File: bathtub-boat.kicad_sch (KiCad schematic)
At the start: 3 parts, among them U1 esp-01m, U2 tp4056

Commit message: Add components
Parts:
- added BT2: Battery_Cell, Connector_JST:JST_PH_S2B-PH-SM4-TB_1x02-1MP_P2.00mm_Horizontal, symbol Device:Battery_Cell
- added BT3: Battery_Cell, Connector_JST:JST_PH_B2B-PH-K_1x02_P2.00mm_Vertical, symbol Device:Battery_Cell
- added J1: I2C, Connector_JST:JST_SH_SM04B-SRSS-TB_1x04-1MP_P1.00mm_Horizontal, symbol Connector_Generic:Conn_01x04
- added J2: SPI, Connector_PinHeader_2.54mm:PinHeader_1x06_P2.54mm_Vertical, symbol Connector_Generic:Conn_01x06
- added SW1: MODE, Button_Switch_SMD:SW_Push_1P1T_NO_Vertical_Wuerth_434133025816, symbol Switch:SW_Push
- added SW2: RESET, Button_Switch_SMD:SW_Push_1P1T_NO_Vertical_Wuerth_434133025816, symbol Switch:SW_Push
- added SW4: A, Button_Switch_SMD:SW_Push_1P1T_NO_Vertical_Wuerth_434133025816, symbol Switch:SW_Push
- added U3: UA78M33_TO252, Package_TO_SOT_SMD:TO-252-2, symbol Regulator_Linear:KA78M05_TO252
- added U4: DS18B20, Package_TO_SOT_THT:TO-92_Inline_Wide, symbol Sensor_Temperature:DS18B20
- added U5: TTL, Connector_PinHeader_2.54mm:PinHeader_1x04_P2.54mm_Vertical, symbol ftdi-connector:TTL
- BT1: footprint (none) -> Connector_JST:JST_GH_BM02B-GHS-TBT_1x02-1MP_P1.25mm_Vertical
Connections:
- net +3V3: now also J1.2 (Pin_2), J2.2 (Pin_2), U3.3 (VO), U4.3 (VDD), U5.4 (VDD)
- net GND: now also U2.2 (IN-), U2.4 (O-), J1.1 (Pin_1), J2.1 (Pin_1), SW1.1, SW2.1, SW4.1, U3.2 (GND), U4.1 (GND), U5.1 (GND)
- net RX: now also U5.3 (TX)
- net TX: now also U5.2 (RX)
- net VBUS: now reaches U2.1 (IN+)
- net +5V: now reaches U2.3 (O+)
- net +5V: now also U3.1 (VI)
- net at BT1.1 (+), U2.5 (B+): now also BT2.1 (+), BT3.1 (+)
- net at BT1.2 (-), U2.6 (B-): now also BT2.2 (-), BT3.2 (-)
- net I2C_SDA: now reaches U1.10 (GP4)
- net I2C_SDA: now also J1.3 (Pin_3)
- net TEMP: now reaches U1.11 (GP9)
- net TEMP: now also U4.2 (DQ)
- net Neopixel: now reaches U1.12 (GP10)
- net I2C_SCL: now reaches U1.13 (GP5)
- net I2C_SCL: now also J1.4 (Pin_4)
- net SPI_MISO: now reaches U1.14 (GP12)
- net SPI_MISO: now also J2.3 (Pin_3)
- net SPI_CLK: now reaches U1.15 (GP14)
- net SPI_CLK: now also J2.5 (Pin_5)
- net at U1.17 (GP16): now also U1.18 (RST), SW2.2
- net SPI_MOSI: now reaches U1.5 (GP13)
- net SPI_MOSI: now also J2.4 (Pin_4)
- net SPI_CS: now reaches U1.6 (GP15)
- net SPI_CS: now also J2.6 (Pin_6)
- net BUTTON-A: now reaches U1.7 (GP2)
- net BUTTON-A: now also SW4.2
- net at U1.8 (GP0): now also SW1.2
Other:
- moved on the sheet: U2

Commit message: Prepare the pcb for next iteration
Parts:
- removed BT2: Battery_Cell, Connector_JST:JST_PH_S2B-PH-SM4-TB_1x02-1MP_P2.00mm_Horizontal, symbol Device:Battery_Cell
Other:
- note added: "TODO: - Lightsensor on ADC - Add a battery Switch - The push button should be on the top side (THT) - Order on JLCPCB?"
- company: (none) -> Besmer Labs
- title: (none) -> BathTubBoat
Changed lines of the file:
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@@
 (kicad_sch (version 20211123) (generator eeschema)
   (paper "A4")
+  (title_block
+    (title "BathTubBoat")
+    (date "2024-01-22")
+    (rev "v1.1-beta")
+    (company "Besmer Labs")
+  )
   (junction (at 148.59 83.82) (diameter 0) (color 0 0 0 0)
   )
   (junction (at 78.74 44.45) (diameter 0) (color 0 0 0 0)
   )
-  (junction (at 72.39 44.45) (diameter 0) (color 0 0 0 0)
-  )
-  (junction (at 72.39 52.07) (diameter 0) (color 0 0 0 0)
-  )
   (junction (at 78.74 52.07) (diameter 0) (color 0 0 0 0)
   )
-  (wire (pts (xy 72.39 44.45) (xy 78.74 44.45))
+  (wire (pts (xy 64.77 44.45) (xy 78.74 44.45))
     (stroke (width 0) (type default) (color 0 0 0 0))
   )
@@
     (stroke (width 0) (type default) (color 0 0 0 0))
   )
-  (wire (pts (xy 72.39 52.07) (xy 78.74 52.07))
-    (stroke (width 0) (type default) (color 0 0 0 0))
-  )
-  (wire (pts (xy 64.77 52.07) (xy 72.39 52.07))
+  (wire (pts (xy 64.77 52.07) (xy 78.74 52.07))
     (stroke (width 0) (type default) (color 0 0 0 0))
   )
@@
     (stroke (width 0) (type default) (color 0 0 0 0))
   )
-  (wire (pts (xy 64.77 44.45) (xy 72.39 44.45))
-    (stroke (width 0) (type default) (color 0 0 0 0))
-  )
   (wire (pts (xy 146.05 83.82) (xy 148.59 83.82))
     (stroke (width 0) (type default) (color 0 0 0 0))
+  )
+  (text "TODO:\n\n- Lightsensor on ADC\n- Add a battery Switch\n- The push button should be on the top side (THT)\n- Order on JLCPCB?"
+    (at 81.28 110.49 0)
+    (effects (font (size 1.27 1.27)) (justify left bottom))
   )
   (global_label "I2C_SDA" (shape input) (at 208.28 59.69 180) (fields_autoplaced)
@@
     (pin "3")
     (pin "4")
-  )
-  (symbol (lib_id "Device:Battery_Cell") (at 72.39 49.53 0) (unit 1)
-    (in_bom yes) (on_board yes)
-    (property "Reference" "BT2" (id 0) (at 58.42 46.99 0)
-      (effects (font (size 1.27 1.27)) (justify left) hide)
-    )
-    (property "Value" "Battery_Cell" (id 1) (at 58.42 49.53 0)
-      (effects (font (size 1.27 1.27)) (justify left) hide)
-    )
-    (property "Footprint" "Connector_JST:JST_PH_S2B-PH-SM4-TB_1x02-1MP_P2.00mm_Horizontal" (id 2) (at 72.39 48.006 90)
-      (effects (font (size 1.27 1.27)) hide)
-    )
-    (property "Datasheet" "~" (id 3) (at 72.39 48.006 90)
-      (effects (font (size 1.27 1.27)) hide)
-    )
-    (pin "1")
-    (pin "2")
   )
   (symbol (lib_id "power:GND") (at 186.69 49.53 0) (mirror y) (unit 1)
@@
       (reference "BT1") (unit 1) (value "Battery_Cell") (footprint "Connector_JST:JST_GH_BM02B-GHS-TBT_1x02-1MP_P1.25mm_Vertical")
     )
-    (path "/156b0c64-d121-48fd-88c7-c592ec9bfc1c"
-      (reference "BT2") (unit 1) (value "Battery_Cell") (footprint "Connector_JST:JST_PH_S2B-PH-SM4-TB_1x02-1MP_P2.00mm_Horizontal")
-    )
     (path "/31f7b8eb-341a-4ba1-bbcd-8710cb8d470a"

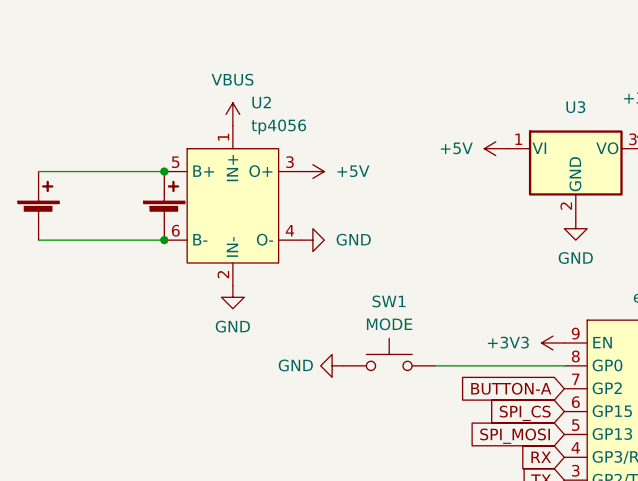
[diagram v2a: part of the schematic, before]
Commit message: Minor changes to board, reflect tp4056 connections, todos for upcoming version
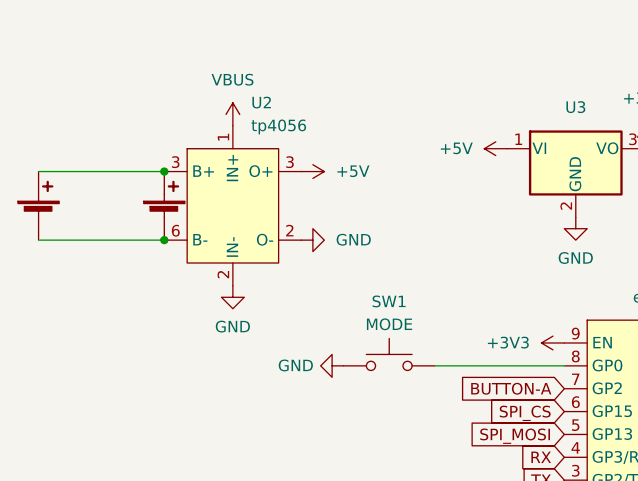
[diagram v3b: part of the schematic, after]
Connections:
- net GND: no longer U2.4 (O-)
- net at BT1.1 (+), BT3.1 (+): now also U2.3 (O+); no longer U2.5 (B+)
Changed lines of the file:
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@@
     (pin "1")
     (pin "2")
+    (pin "2")
     (pin "3")
-    (pin "4")
-    (pin "5")
+    (pin "3")
     (pin "6")
   )

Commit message: New PCB version 2.0
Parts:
- removed BT1: Battery_Cell, Connector_JST:JST_GH_BM02B-GHS-TBT_1x02-1MP_P1.25mm_Vertical, symbol Device:Battery_Cell
- removed U4: DS18B20, Package_TO_SOT_THT:TO-92_Inline_Wide, symbol Sensor_Temperature:DS18B20
- added D1: WS2812B, LED_THT:LED_D5.0mm-4_RGB_Wide_Pins, symbol LED:WS2812B
- added H1, H2, H3: MountingHole, MountingHole:MountingHole_3.2mm_M3, symbol Mechanical:MountingHole
- added J3: I2C, Connector_PinHeader_2.54mm:PinHeader_1x04_P2.54mm_Vertical, symbol Connector_Generic:Conn_01x04
- added J4: DS18B20, Connector_JST:JST_XH_B3B-XH-A_1x03_P2.50mm_Vertical, symbol Connector_Generic:Conn_01x03
- added SW3: POWER, Connector_PinHeader_2.54mm:PinHeader_1x03_P2.54mm_Vertical, symbol Switch:SW_SPDT
- added TP1: ADC, TestPoint:TestPoint_THTPad_2.0x2.0mm_Drill1.0mm, symbol Connector:TestPoint
- added U6: magnetic-charger, magnetic-charger:magnetic-charger, symbol magnetic-charger:magnetic-charger
- SW1, SW2, SW4: footprint Button_Switch_SMD:SW_Push_1P1T_NO_Vertical_Wuerth_434133025816 -> pts636:pts636
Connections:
- net TEMP is gone; now on net Neopixel: U1.11 (GP9)
- net +3V3: now also J3.2 (Pin_2), J4.1 (Pin_1)
- net +5V: now also D1.1 (VDD), SW3.2 (B); no longer U2.3 (O+)
- net GND: now also U2.6 (O-), D1.3 (VSS), J3.1 (Pin_1), J4.3 (Pin_3), U6.1 (GND)
- net I2C_SCL: now also J3.4 (Pin_4)
- net I2C_SDA: now also U1.12 (GP10), J3.3 (Pin_3); no longer U1.10 (GP4)
- net Neopixel: now also D1.4 (DIN); no longer U1.12 (GP10)
- net VBUS: now also U6.2 (VCC)
- net BAT+: now reaches BT3.1 (+), U2.3 (B+)
- net BAT+: now also U2.5 (O+), SW3.3 (C)
- net BAT-: now reaches BT3.2 (-)
- net BAT-: now also U2.4 (B-); no longer U2.6 (B-)
- net at U1.16 (ADC): now also TP1.1
- net BUTTON-A: no longer names the net of SW4.2, U1.7 (GP2)
- new net Temp: J4.2 (Pin_2), U1.10 (GP4)
- no-connect marks 0 -> 2
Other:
- note removed: "TODO: - Lightsensor on ADC - Add a battery Switch - The push button should be on the top side (THT) - Order on JLCPCB?"
- moved on the sheet: J1, J2, SW1, SW2, SW4, U1, U2, U3, U5

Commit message: Add power switch
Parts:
- SW3: footprint Connector_PinHeader_2.54mm:PinHeader_1x03_P2.54mm_Vertical -> as12ap:as12ap
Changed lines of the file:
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@@
     (property "Reference" "SW3" (id 0) (at 102.87 53.34 0))
     (property "Value" "POWER" (id 1) (at 102.87 55.88 0))
-    (property "Footprint" "Connector_PinHeader_2.54mm:PinHeader_1x03_P2.54mm_Vertical" (id 2) (at 102.87 60.96 0)
+    (property "Footprint" "as12ap:as12ap" (id 2) (at 102.87 60.96 0)
       (effects (font (size 1.27 1.27)) hide)
     )
@@
     )
     (path "/22efc92b-b9be-4db4-9841-9ce20d95d505"
-      (reference "SW3") (unit 1) (value "POWER") (footprint "Connector_PinHeader_2.54mm:PinHeader_1x03_P2.54mm_Vertical")
+      (reference "SW3") (unit 1) (value "POWER") (footprint "as12ap:as12ap")
     )
     (path "/51a0c016-46fc-4088-9ec6-8953b40e18ca"

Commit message: Prepare for milling
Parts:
- added C1, C2: C_Polarized_Small, Capacitor_THT:CP_Radial_D5.0mm_P2.50mm, symbol Device:C_Polarized_Small
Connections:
- net +3V3: now also C2.1
- net +5V: now also C1.1
- net GND: now also C1.2, C2.2
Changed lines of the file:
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@@
     (company "Besmer Labs")
   )
+  (junction (at 154.94 67.31) (diameter 0) (color 0 0 0 0)
+  )
   (junction (at 171.45 109.22) (diameter 0) (color 0 0 0 0)
   )
   (junction (at 82.55 63.5) (diameter 0) (color 0 0 0 0)
+  )
+  (junction (at 139.7 67.31) (diameter 0) (color 0 0 0 0)
   )
   (junction (at 97.79 63.5) (diameter 0) (color 0 0 0 0)
@@
     (pin "2")
   )
+  (symbol (lib_id "Device:C_Polarized_Small") (at 154.94 69.85 0) (unit 1)
+    (in_bom yes) (on_board yes) (fields_autoplaced)
+    (property "Reference" "C2" (id 0) (at 157.48 68.0338 0)
+      (effects (font (size 1.27 1.27)) (justify left))
+    )
+    (property "Value" "C_Polarized_Small" (id 1) (at 157.48 70.5738 0)
+      (effects (font (size 1.27 1.27)) (justify left))
+    )
+    (property "Footprint" "Capacitor_THT:CP_Radial_D5.0mm_P2.50mm" (id 2) (at 154.94 69.85 0)
+      (effects (font (size 1.27 1.27)) hide)
+    )
+    (property "Datasheet" "~" (id 3) (at 154.94 69.85 0)
+      (effects (font (size 1.27 1.27)) hide)
+    )
+    (pin "1")
+    (pin "2")
+  )
+  (symbol (lib_id "power:GND") (at 139.7 72.39 0) (unit 1)
+    (in_bom yes) (on_board yes) (fields_autoplaced)
+    (property "Reference" "#PWR0128" (id 0) (at 139.7 78.74 0)
+      (effects (font (size 1.27 1.27)) hide)
+    )
+    (property "Value" "GND" (id 1) (at 139.7 76.962 0))
+    (property "Footprint" "" (id 2) (at 139.7 72.39 0)
+      (effects (font (size 1.27 1.27)) hide)
+    )
+    (property "Datasheet" "" (id 3) (at 139.7 72.39 0)
+      (effects (font (size 1.27 1.27)) hide)
+    )
+    (pin "1")
+  )
   (symbol (lib_id "Connector_Generic:Conn_01x03") (at 205.74 71.12 0) (unit 1)
     (in_bom yes) (on_board yes) (fields_autoplaced)
@@
     )
     (property "Datasheet" "" (id 3) (at 55.88 66.04 0)
+      (effects (font (size 1.27 1.27)) hide)
+    )
+    (pin "1")
+  )
+  (symbol (lib_id "power:GND") (at 154.94 72.39 0) (unit 1)
+    (in_bom yes) (on_board yes) (fields_autoplaced)
+    (property "Reference" "#PWR0129" (id 0) (at 154.94 78.74 0)
+      (effects (font (size 1.27 1.27)) hide)
+    )
+    (property "Value" "GND" (id 1) (at 154.94 76.962 0))
+    (property "Footprint" "" (id 2) (at 154.94 72.39 0)
+      (effects (font (size 1.27 1.27)) hide)
+    )
+    (property "Datasheet" "" (id 3) (at 154.94 72.39 0)
       (effects (font (size 1.27 1.27)) hide)
     )
@@
     (pin "1")
   )
+  (symbol (lib_id "Device:C_Polarized_Small") (at 139.7 69.85 0) (unit 1)
+    (in_bom yes) (on_board yes) (fields_autoplaced)
+    (property "Reference" "C1" (id 0) (at 142.24 68.0338 0)
+      (effects (font (size 1.27 1.27)) (justify left))
+    )
+    (property "Value" "C_Polarized_Small" (id 1) (at 142.24 70.5738 0)
+      (effects (font (size 1.27 1.27)) (justify left))
+    )
+    (property "Footprint" "Capacitor_THT:CP_Radial_D5.0mm_P2.50mm" (id 2) (at 139.7 69.85 0)
+      (effects (font (size 1.27 1.27)) hide)
+    )
+    (property "Datasheet" "~" (id 3) (at 139.7 69.85 0)
+      (effects (font (size 1.27 1.27)) hide)
+    )
+    (pin "1")
+    (pin "2")
+  )
   (symbol (lib_id "power:+3V3") (at 208.28 97.79 90) (unit 1)
     (in_bom yes) (on_board yes)
@@
       (reference "#PWR0127") (unit 1) (value "GND") (footprint "")
     )
+    (path "/806cc8ef-77fc-4a85-9bcc-7a2d0db5aca0"
+      (reference "#PWR0128") (unit 1) (value "GND") (footprint "")
+    )
+    (path "/adda9f23-fd8e-497a-b0be-1a745a2a15d8"
+      (reference "#PWR0129") (unit 1) (value "GND") (footprint "")
+    )
     (path "/31f7b8eb-341a-4ba1-bbcd-8710cb8d470a"
       (reference "BT3") (unit 1) (value "Battery_Cell") (footprint "Connector_JST:JST_PH_B2B-PH-K_1x02_P2.00mm_Vertical")
     )
+    (path "/fbe8dd77-34d2-4e2a-a537-658ddee48b76"
+      (reference "C1") (unit 1) (value "C_Polarized_Small") (footprint "Capacitor_THT:CP_Radial_D5.0mm_P2.50mm")
+    )
+    (path "/7f835ca6-718a-4dfe-92e0-14d26cbb7058"
+      (reference "C2") (unit 1) (value "C_Polarized_Small") (footprint "Capacitor_THT:CP_Radial_D5.0mm_P2.50mm")
+    )
     (path "/e1a27634-5941-4abc-b59b-6fdbe072b5b0"

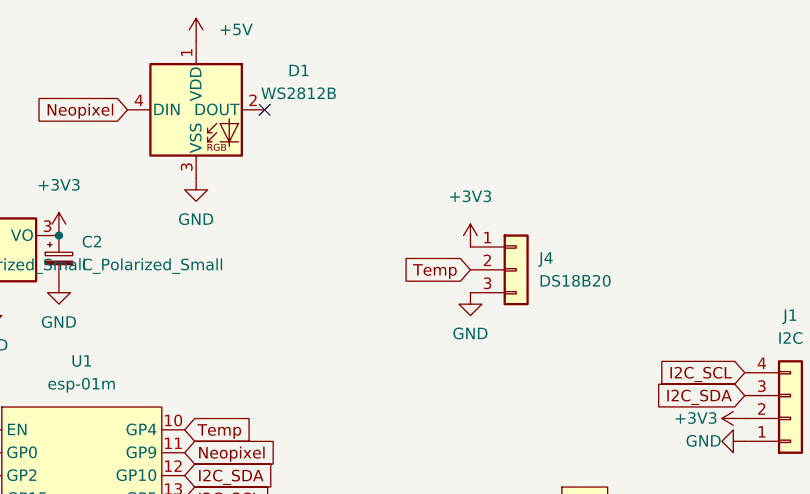
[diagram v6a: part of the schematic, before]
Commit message: Add pullup resistor for optional parasitic power
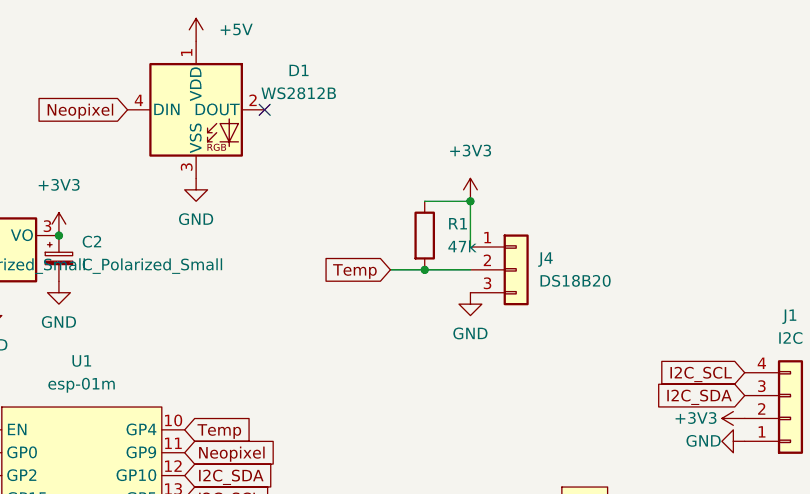
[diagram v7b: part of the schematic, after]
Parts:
- added R1: 47k, Resistor_THT:R_Axial_DIN0204_L3.6mm_D1.6mm_P1.90mm_Vertical, symbol Device:R
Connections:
- net +3V3: now also R1.1
- net Temp: now also R1.2
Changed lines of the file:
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@@
   (junction (at 139.7 67.31) (diameter 0) (color 0 0 0 0)
   )
+  (junction (at 195.58 71.12) (diameter 0) (color 0 0 0 0)
+  )
   (junction (at 97.79 63.5) (diameter 0) (color 0 0 0 0)
+  )
+  (junction (at 200.66 63.5) (diameter 0) (color 0 0 0 0)
   )
   (no_connect (at 177.8 53.34))
@@
     (stroke (width 0) (type default) (color 0 0 0 0))
   )
+  (wire (pts (xy 195.58 63.5) (xy 200.66 63.5))
+    (stroke (width 0) (type default) (color 0 0 0 0))
+  )
+  (wire (pts (xy 191.77 71.12) (xy 195.58 71.12))
+    (stroke (width 0) (type default) (color 0 0 0 0))
+  )
   (wire (pts (xy 82.55 59.69) (xy 82.55 63.5))
     (stroke (width 0) (type default) (color 0 0 0 0))
@@
     (stroke (width 0) (type default) (color 0 0 0 0))
   )
+  (wire (pts (xy 200.66 63.5) (xy 200.66 68.58))
+    (stroke (width 0) (type default) (color 0 0 0 0))
+  )
   (wire (pts (xy 97.79 63.5) (xy 97.79 59.69))
     (stroke (width 0) (type default) (color 0 0 0 0))
@@
   )
   (wire (pts (xy 68.58 71.12) (xy 82.55 71.12))
+    (stroke (width 0) (type default) (color 0 0 0 0))
+  )
+  (wire (pts (xy 195.58 71.12) (xy 200.66 71.12))
     (stroke (width 0) (type default) (color 0 0 0 0))
   )
@@
     )
   )
-  (global_label "Temp" (shape input) (at 200.66 71.12 180) (fields_autoplaced)
-    (effects (font (size 1.27 1.27)) (justify right))
-    (property "Intersheet References" "${INTERSHEET_REFS}" (id 0) (at 193.3483 71.0406 0)
+  (global_label "Temp" (shape input) (at 191.77 71.12 180) (fields_autoplaced)
+    (effects (font (size 1.27 1.27)) (justify right))
+    (property "Intersheet References" "${INTERSHEET_REFS}" (id 0) (at 184.4583 71.0406 0)
       (effects (font (size 1.27 1.27)) (justify right) hide)
     )
@@
     (pin "1")
   )
-  (symbol (lib_id "power:+3V3") (at 200.66 68.58 0) (mirror y) (unit 1)
-    (in_bom yes) (on_board yes) (fields_autoplaced)
-    (property "Reference" "#PWR0112" (id 0) (at 200.66 72.39 0)
-      (effects (font (size 1.27 1.27)) hide)
-    )
-    (property "Value" "+3V3" (id 1) (at 200.66 62.992 0))
-    (property "Footprint" "" (id 2) (at 200.66 68.58 0)
-      (effects (font (size 1.27 1.27)) hide)
-    )
-    (property "Datasheet" "" (id 3) (at 200.66 68.58 0)
+  (symbol (lib_id "power:+3V3") (at 200.66 63.5 0) (mirror y) (unit 1)
+    (in_bom yes) (on_board yes) (fields_autoplaced)
+    (property "Reference" "#PWR0112" (id 0) (at 200.66 67.31 0)
+      (effects (font (size 1.27 1.27)) hide)
+    )
+    (property "Value" "+3V3" (id 1) (at 200.66 57.912 0))
+    (property "Footprint" "" (id 2) (at 200.66 63.5 0)
+      (effects (font (size 1.27 1.27)) hide)
+    )
+    (property "Datasheet" "" (id 3) (at 200.66 63.5 0)
       (effects (font (size 1.27 1.27)) hide)
     )
@@
     (pin "5")
     (pin "6")
+  )
+  (symbol (lib_id "Device:R") (at 195.58 67.31 0) (unit 1)
+    (in_bom yes) (on_board yes) (fields_autoplaced)
+    (property "Reference" "R1" (id 0) (at 198.12 66.0399 0)
+      (effects (font (size 1.27 1.27)) (justify left))
+    )
+    (property "Value" "47k" (id 1) (at 198.12 68.5799 0)
+      (effects (font (size 1.27 1.27)) (justify left))
+    )
+    (property "Footprint" "Resistor_THT:R_Axial_DIN0204_L3.6mm_D1.6mm_P1.90mm_Vertical" (id 2) (at 193.802 67.31 90)
+      (effects (font (size 1.27 1.27)) hide)
+    )
+    (property "Datasheet" "~" (id 3) (at 195.58 67.31 0)
+      (effects (font (size 1.27 1.27)) hide)
+    )
+    (pin "1")
+    (pin "2")
   )
   (symbol (lib_id "Connector:TestPoint") (at 168.91 104.14 270) (unit 1)
@@
       (reference "J4") (unit 1) (value "DS18B20") (footprint "Connector_JST:JST_XH_B3B-XH-A_1x03_P2.50mm_Vertical")
     )
+    (path "/4ee60417-128e-409c-b03b-68efa1098f9b"
+      (reference "R1") (unit 1) (value "47k") (footprint "Resistor_THT:R_Axial_DIN0204_L3.6mm_D1.6mm_P1.90mm_Vertical")
+    )
     (path "/7f4edab6-b5b3-4188-91f7-4f76ddc427d3"
